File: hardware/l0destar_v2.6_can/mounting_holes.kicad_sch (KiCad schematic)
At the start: 4 parts

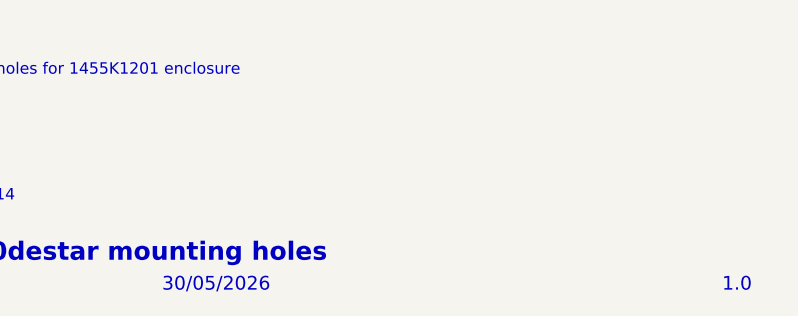
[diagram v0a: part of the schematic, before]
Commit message: fix sheet annotations
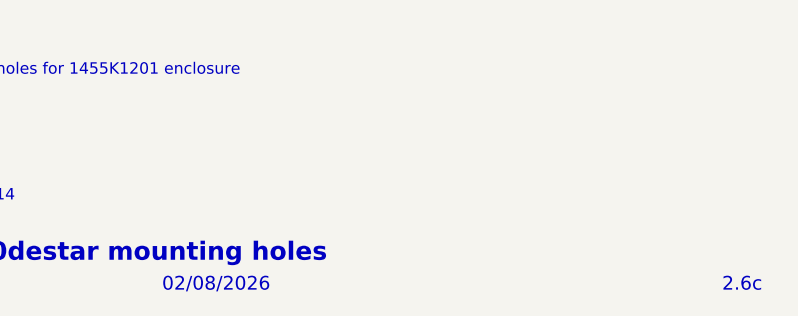
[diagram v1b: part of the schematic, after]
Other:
- note added: "02/08/2026"
- note added: "2.6c"
- note removed: "1.0"
- note removed: "30/05/2026"
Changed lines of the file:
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@@
 		)
 	)
-	(text "1.0"
+	(text "2.6c"
 		(exclude_from_sim no)
 		(at 268.478 193.294 0)
@@
 		)
 	)
-	(text "30/05/2026"
+	(text "02/08/2026"
 		(exclude_from_sim no)
 		(at 206.248 193.294 0)
